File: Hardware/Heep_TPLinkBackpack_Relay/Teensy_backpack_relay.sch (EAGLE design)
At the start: 37 parts, among them Q2 600mA/40V, U1 ENC28J60-SSOP

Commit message: #44 Finalized TPLink Backpack Schematics and Layouts
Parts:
- removed JP3, JP5, JP7: (no value), SparkFun-Connectors:M05X2NO_SILK
- added D4, D5: 200mA/100V/1V, adafruit:DIODESOD-123
- added JP11, JP12: (no value), microbuilder:HEADER-1X3_508TERM
- added JP13, JP14, JP15: (no value), SparkFun-Connectors:M04X2
- added K1, K2: G5LE, relay:G5LE
- added Q1, Q4: MMBT2222, microbuilder:TRANSISTOR_NPN
- added R10, R12: 10K, microbuilder:RESISTOR0805_NOOUTLINE
- added R11, R9: 1K, microbuilder:RESISTOR0805_NOOUTLINE
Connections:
- removed net N$20: BREAKOUT1.4, U$1.23/A9/T/PWM
- removed net N$21: BREAKOUT1.5, U$1.22/A8/T/PWM
- new net N$30: D5.A, K21.2, Q4.C
- new net N$31: JP11.1, K12.S
- new net N$32: JP11.3, K12.O
- new net N$33: JP11.2, K12.P
- new net N$34: Q1.B, R10.2, R9.2
- new net N$35: JP12.1, K22.S
- new net N$36: JP12.3, K22.O
- new net N$37: JP12.2, K22.P
- new net N$38: D4.A, K11.2, Q1.C
- new net N$39: Q4.B, R11.2, R12.2
- new net RELAY_L: BREAKOUT1.5, R9.1, U$1.22/A8/T/PWM
- new net RELAY_R: BREAKOUT1.4, R11.1, U$1.23/A9/T/PWM
- net 3.3V: now also D4.C, D5.C, K11.1, K21.1
- net AGND: now also Q1.E, Q4.E, R10.1, R12.1
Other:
- note added: "Left Relay"
- note added: "Right Relay"

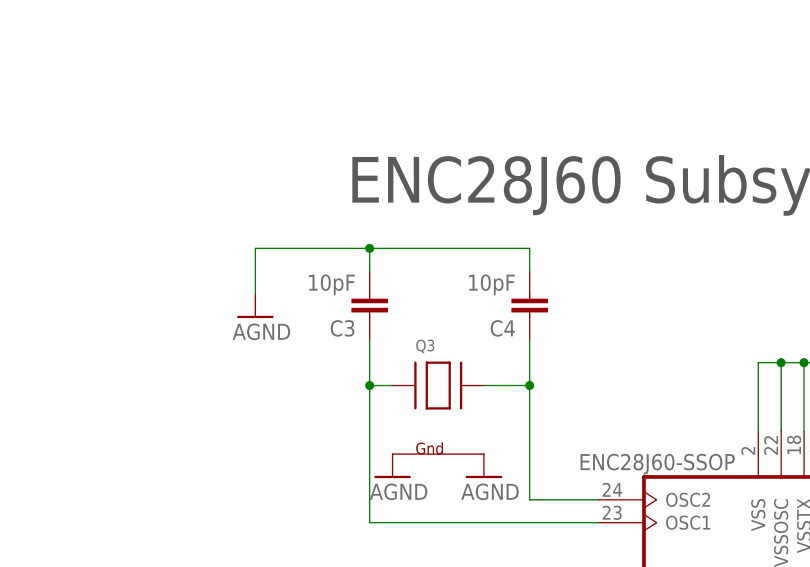
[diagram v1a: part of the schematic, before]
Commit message: #260 Change teensy capacitors to 8pf
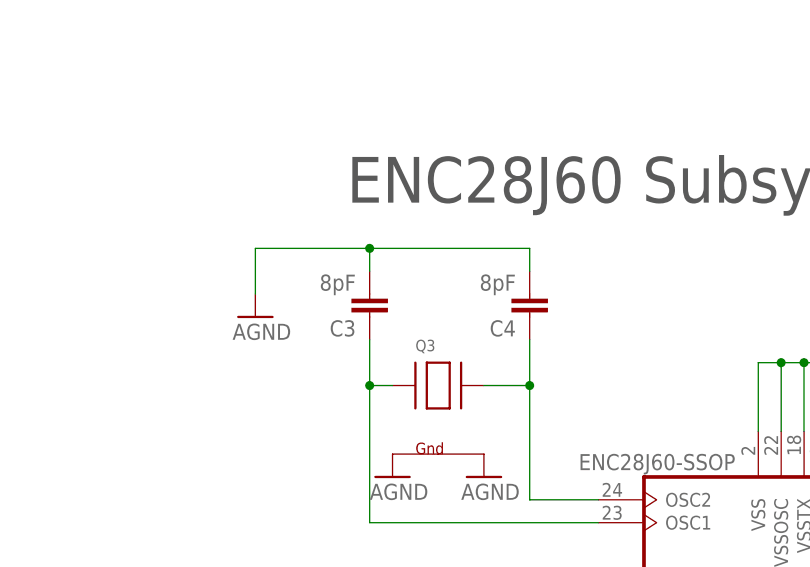
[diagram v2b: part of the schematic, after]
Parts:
- C3, C4: value 10pF -> 8pF
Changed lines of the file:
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@@
 <part name="R3" library="SparkFun-Resistors" deviceset="RESISTOR" device="0603" value="51"/>
 <part name="R4" library="SparkFun-Resistors" deviceset="RESISTOR" device="0603" value="51"/>
-<part name="C3" library="SparkFun-Passives" deviceset="CAP" device="0603-CAP" value="10pF"/>
-<part name="C4" library="SparkFun-Passives" deviceset="CAP" device="0603-CAP" value="10pF"/>
+<part name="C3" library="SparkFun-Passives" deviceset="CAP" device="0603-CAP" value="8pF"/>
+<part name="C4" library="SparkFun-Passives" deviceset="CAP" device="0603-CAP" value="8pF"/>
 <part name="SUPPLY1" library="SparkFun-Aesthetics" deviceset="3.3V" device=""/>
 <part name="C5" library="SparkFun-Capacitors" deviceset="CAP" device="0603-CAP" value="0.1uF"/>
